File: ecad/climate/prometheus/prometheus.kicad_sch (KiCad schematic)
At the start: 6 parts, among them J1 2.5mm I.D. 5.5mm O.D., J2 JST PH, J3 JST PH, J4 Phoenix MCV_1,5

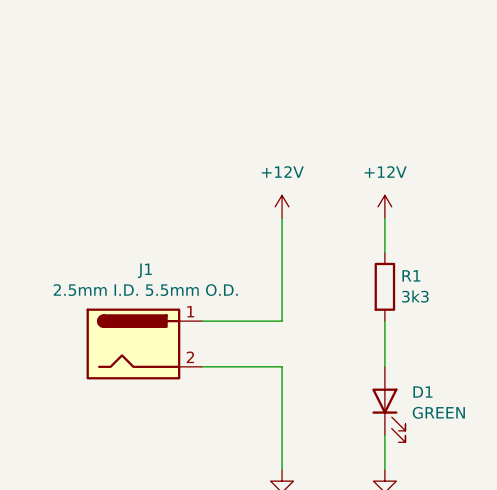
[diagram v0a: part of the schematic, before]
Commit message: [WIP] Switches to kicad 9
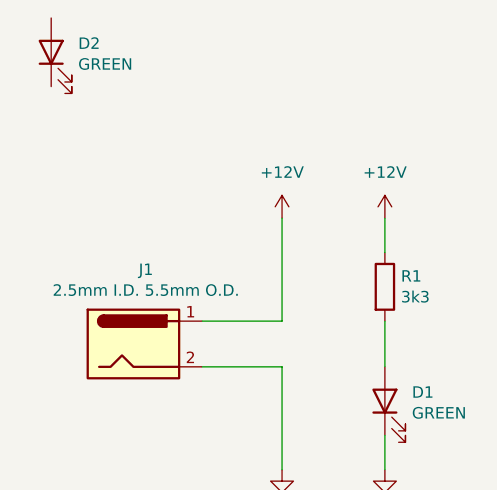
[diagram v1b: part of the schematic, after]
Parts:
- added D2: GREEN, LED_SMD:LED_0603_1608Metric, symbol Device:LED
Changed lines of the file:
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@@
 (kicad_sch
-	(version 20231120)
+	(version 20250114)
 	(generator "eeschema")
-	(generator_version "8.0")
+	(generator_version "9.0")
 	(paper "A5")
 	(wire
@@
 	(label "CAN+"
 		(at 95.25 40.64 180)
-		(fields_autoplaced yes)
 		(effects
 			(font
@@
 	(label "CAN-"
 		(at 95.25 43.18 180)
-		(fields_autoplaced yes)
 		(effects
 			(font
@@
 	(label "CAN+"
 		(at 125.73 40.64 180)
-		(fields_autoplaced yes)
 		(effects
 			(font
@@
 	(label "CAN-"
 		(at 125.73 43.18 180)
-		(fields_autoplaced yes)
 		(effects
 			(font
@@
 	)
 	(symbol
+		(lib_id "Device:LED")
+		(at 27.691 19.6597 90)
+		(unit 1)
+		(exclude_from_sim no)
+		(in_bom yes)
+		(on_board yes)
+		(dnp no)
+		(property "Reference" "D2"
+			(at 30.6882 18.6945 90)
+			(effects
+				(font
+					(size 1.27 1.27)
+				)
+				(justify right)
+			)
+		)
+		(property "Value" "GREEN"
+			(at 30.6882 21.0059 90)
+			(effects
+				(font
+					(size 1.27 1.27)
+				)
+				(justify right)
+			)
+		)
+		(property "Footprint" "LED_SMD:LED_0603_1608Metric"
+			(at 27.691 19.6597 0)
+			(effects
+				(font
+					(size 1.27 1.27)
+				)
+				(hide yes)
+			)
+		)
+		(property "Datasheet" "~"
+			(at 27.691 19.6597 0)
+			(effects
+				(font
+					(size 1.27 1.27)
+				)
+				(hide yes)
+			)
+		)
+		(property "Description" ""
+			(at 27.691 19.6597 0)
+			(effects
+				(font
+					(size 1.27 1.27)
+				)
+				(hide yes)
+			)
+		)
+		(property "MPN" "150060VS75000"
+			(at 27.691 19.6597 0)
+			(effects
+				(font
+					(size 1.27 1.27)
+				)
+				(hide yes)
+			)
+		)
+		(pin "1"
+		)
+		(pin "2"
+		)
+		(instances
+			(project "prometheus"
+				(path "/57607949-2c9f-479e-9874-a3527c8b2083"
+					(reference "D2")
+					(unit 1)
+				)
+			)
+		)
+	)
+	(symbol
 		(lib_id "Connector_Generic:Conn_01x04")
 		(at 107.95 38.1 0)
@@
 		)
 	)
+	(embedded_fonts no)
 )
